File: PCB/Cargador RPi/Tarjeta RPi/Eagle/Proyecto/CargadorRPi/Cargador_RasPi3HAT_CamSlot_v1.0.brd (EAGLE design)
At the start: 65 x 56 mm, 22 parts, among them J2 PIN20X2, U1 MCP3208, X2 22-23-2081

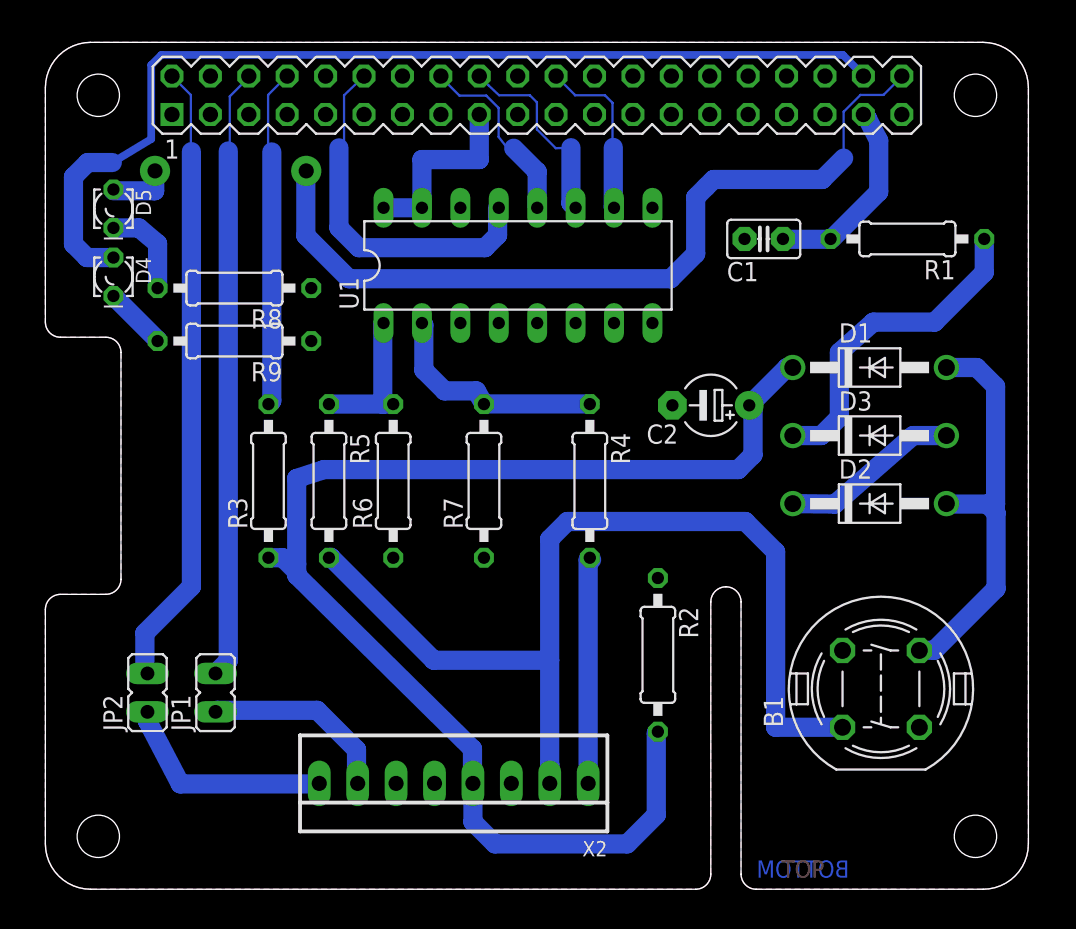
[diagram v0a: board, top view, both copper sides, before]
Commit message: Ajustes para fabricación de PCB.
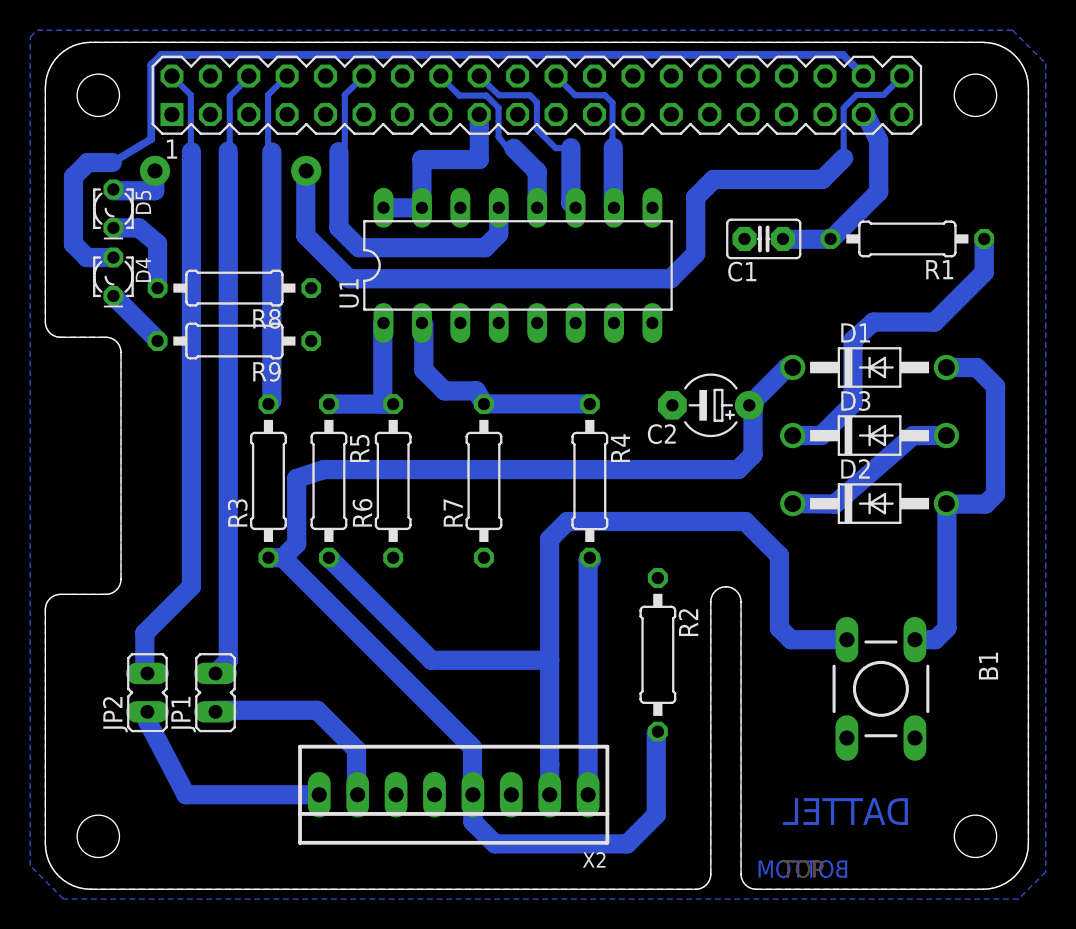
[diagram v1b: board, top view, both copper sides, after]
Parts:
- B1: value DT6 -> DTS-6; device switch-misc:DT6 -> switch-tact:DTS-6
- moved X2 0.75 mm to (27.0, 6.25)
- turned B1 to 270 degrees
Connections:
- removed net DGND: U1.DGND
- net GND: now also U1.DGND
- net N$16: now also B1.3; no longer B1.1
- net N$24: now also B1.1; no longer B1.3
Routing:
- net N$16: track 65.9 -> 60.5 mm
- net N$24: track 27.4 -> 25.1 mm
- net N$17: track 12.7 -> 13.5 mm
- net N$15: track 15.3 -> 16.0 mm
- net N$26: track 86.9 -> 86.3 mm
- net N$6: track 58.0 -> 57.4 mm
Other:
- board text added: "DATTEL"
